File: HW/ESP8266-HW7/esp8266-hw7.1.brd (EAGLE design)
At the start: 58 x 52 mm, 31 parts, among them IC1 MCP1703CB, IC2 ATECC608A-SSHDA-B, IC3 DS18B20U+, J2 Sensors2, J3 Analog, J4 Sensors1, J5 Enable, J6 PGM, J9 Pwr sw, T1 BSS138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

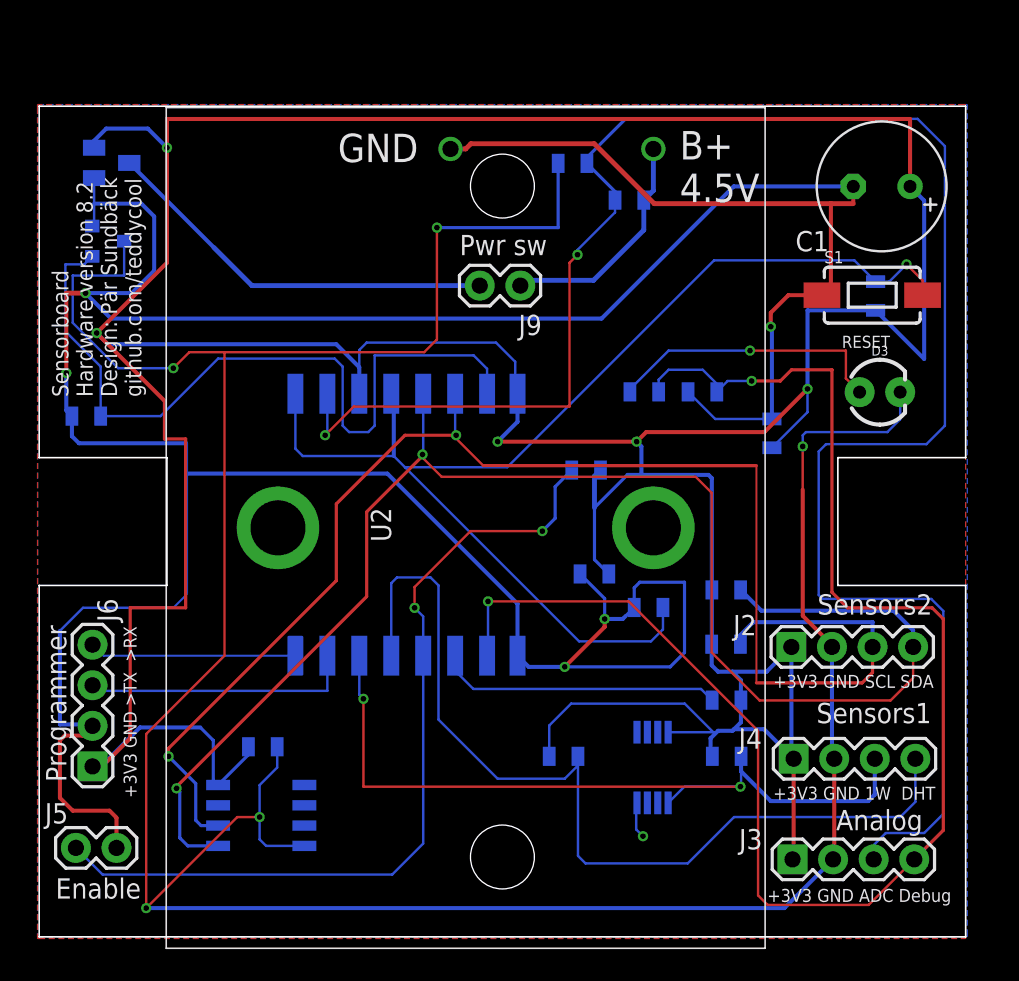
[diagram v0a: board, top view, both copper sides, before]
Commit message: New pcb releases and some updated software
New (final?) releases of pcbs for version 7 and 8. New test program to run for test of the built hardware.
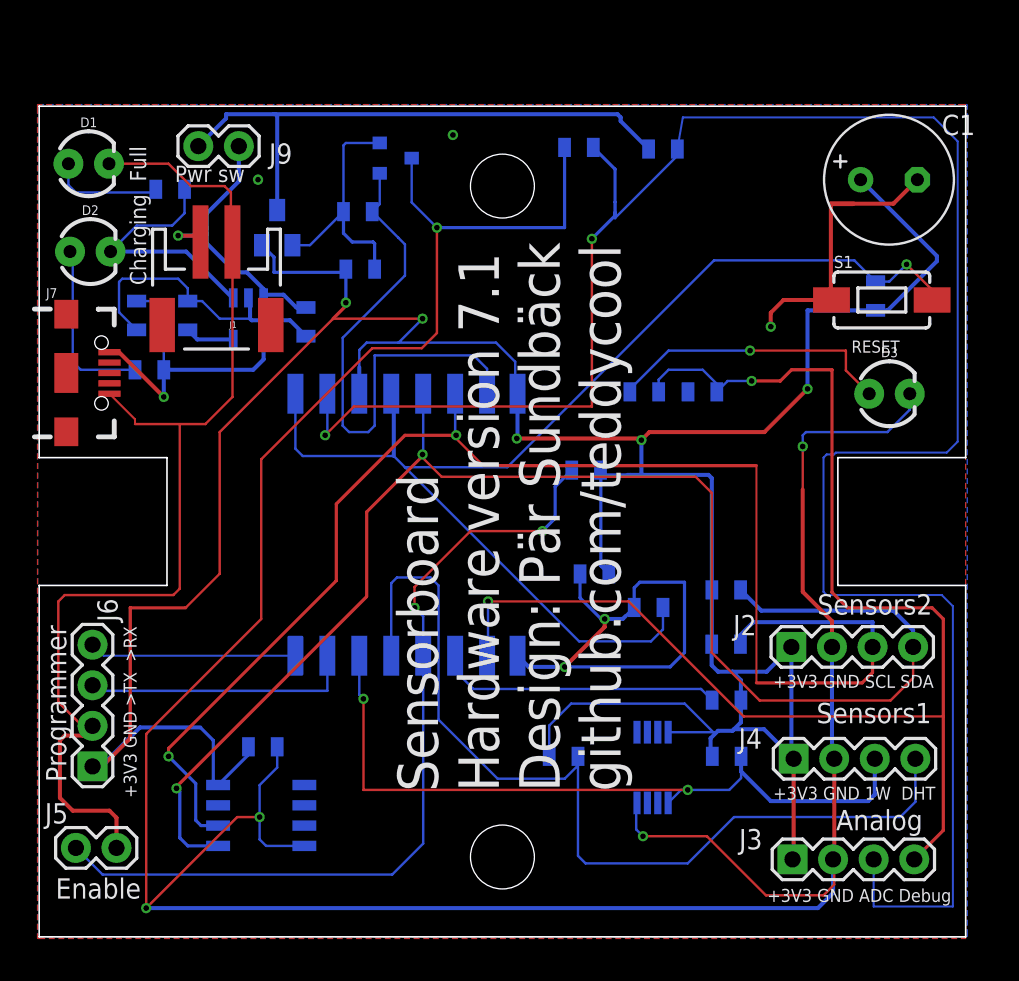
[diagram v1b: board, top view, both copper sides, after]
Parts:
- added C12, C13: 4.7u, SparkFun-Passives:0805
- added D1, D2: (no value), SparkFun-LED:LED_3MM
- added J1: J1, SparkFun-Connectors:JST-2-SMD
- added J7: PWR, SparkFun-Connectors:USB-AB-MICRO-SMD
- added R11: 2k, SparkFun-Resistors:0805
- added R13, R15: 470, SparkFun-Resistors:0805
- U2: value 2479 -> MCP73831; device SamacSys_Parts:2479 -> SparkFun-IC-Power:SOT23-5
- moved C2 27.7 mm to (20.1, 41.8), turned to 180 degrees
- moved R1 21.3 mm to (19.9, 45.4)
- moved J9 19.7 mm to (12.5, 49.5)
- moved U2 18.9 mm to (13.1, 38.7), flipped to the bottom, turned to 180 degrees
- moved T1 18.7 mm to (22.3, 48.8)
- moved IC1 11.1 mm to (14.9, 44.4), turned to 0 degrees
- moved R5 3.83 mm to (39.0, 49.3), turned to 0 degrees
- moved R12 1.08 mm to (33.8, 49.4)
- moved S1 0.67 mm to (52.8, 39.9)
- moved C1 0.62 mm to (53.2, 47.4), turned to 0 degrees
- moved D3 0.61 mm to (53.2, 34.0)
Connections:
- new net N$10: R11.1, U2.5
- new net N$2: D1.A, R13.1
- new net N$3: D2.A, R15.1
- new net STAT: D2.K, R13.2, U2.1
- new net USB+: C12.2, J7.VBUS1, R15.2, U2.4
- net B+: now also C13.2, J1.2, U2.3; no longer R5.2, U2.1
- net GND: now also C12.1, C13.1, D1.K, J1.1, J7.GND1, R11.2
- net PWR: now also R5.2
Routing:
- net GND: track 230.8 -> 150.5 mm, vias 5 -> 4
- net +3V3: track 286.0 -> 205.8 mm
- net USB+: track 0.00 -> 19.6 mm, vias 0 -> 1
- net STAT: track 0.00 -> 16.0 mm
- net SPC: track 48.5 -> 34.1 mm
- net ADC: track 122.5 -> 135.6 mm
- net PWR: track 25.1 -> 36.2 mm
- net N$3: track 0.00 -> 11.1 mm
- net GPIO15: track 95.9 -> 85.6 mm
- net N$2: track 0.00 -> 7.08 mm
- net B+: track 14.5 -> 18.6 mm, vias 0 -> 1
- net N$10: track 0.00 -> 3.10 mm
- net 1W: track 50.3 -> 47.9 mm
- net SPW: track 189.3 -> 187.7 mm, vias 6 -> 5
- net RST: track 77.2 -> 77.7 mm
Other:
- board text added: "Charging Full"
- board text added: "Sensorboard Hardware version 7.1 Design: Pär Sundbäck github.com/teddycool"
- board text removed: "B+ 4.5V"
- board text removed: "B+ 4.5V 3xAAA"
- board text removed: "GND"
- board text removed: "Sensorboard Hardware version 8.2 Design: Pär Sundbäck github.com/teddycool"
